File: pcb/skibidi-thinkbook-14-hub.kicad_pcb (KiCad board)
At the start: 4 copper layers, 40 x 70 mm, 121 parts, among them CN1 PJ-325C5-G, U1 HC-USB3.0-C26, U2 TUSB8042AIRGCR, U3 RTL8153B-VB-CG, U4 CH334P, U5 AP63203WU-7, U6 CYA0650-4.7UH, U7 PCM2704CDBR, Y1 24Mhz, Y2 25Mhz, Y3 12Mhz

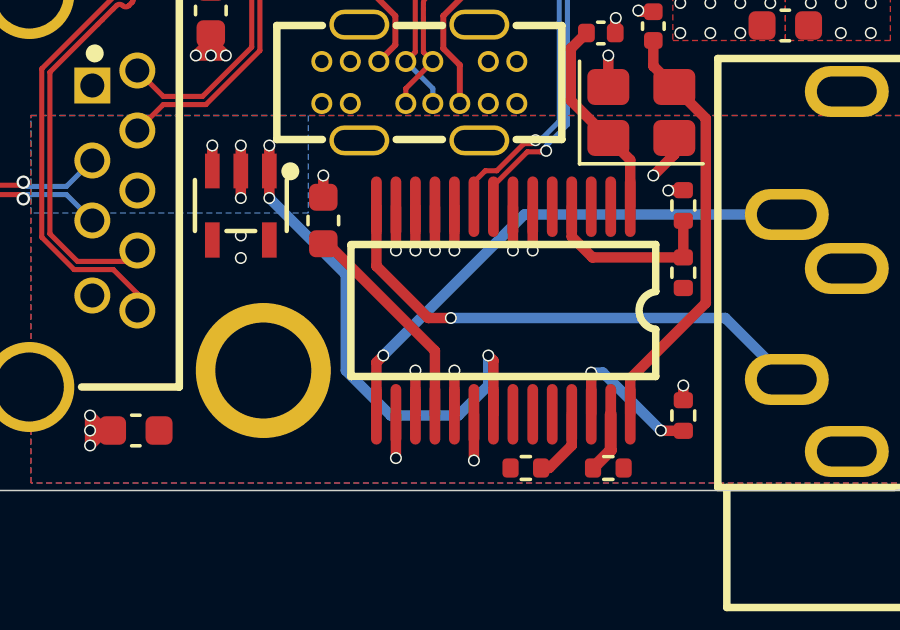
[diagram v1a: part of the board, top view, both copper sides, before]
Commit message: added bom to readme, completed project
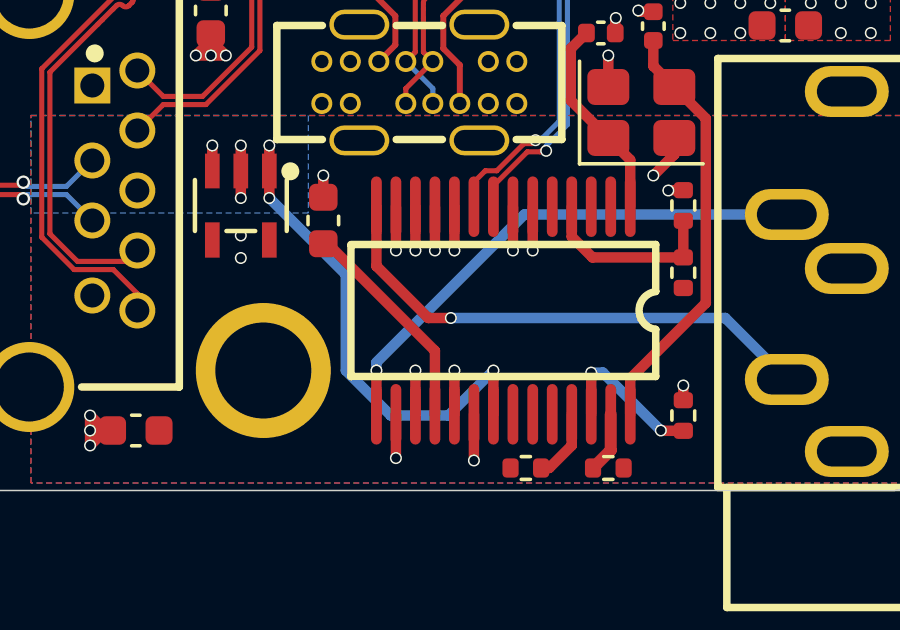
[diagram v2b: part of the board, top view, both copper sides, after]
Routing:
- net VBUS: track 53.4 -> 52.2 mm
